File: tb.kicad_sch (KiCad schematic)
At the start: 66 parts, among them U4 JHL6340SLLSQ, U5 MX25L8006EM1I-12G, U6 SI52112-B6-GT, Y1 ABM8G-25.000MHZ-B4Y-T, Y2 ABM8G-25.000MHZ-B4Y-T

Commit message: Fixed all DRC errors and warnings, finished designators' placement
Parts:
- U5: footprint antmicro-footprints:SOIC-8_W3.9mm -> antmicro-footprints:SOIC-8_3.9x4.9x1.75mm_P1.27mm
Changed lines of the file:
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@@
       (effects (font (size 1.27 1.27) (thickness 0.15)) (justify left))
     )
-    (property "Footprint" "antmicro-footprints:SOIC-8_W3.9mm" (id 2) (at 39.37 384.81 0)
+    (property "Footprint" "antmicro-footprints:SOIC-8_3.9x4.9x1.75mm_P1.27mm" (id 2) (at 39.37 384.81 0)
       (effects (font (size 1.27 1.27) (thickness 0.15)) (justify left bottom) hide)
     )

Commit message: Bump revision, update naming
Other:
- title: (none) -> Thunderbolt to PCIe bridge
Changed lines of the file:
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@@
   (paper "A3" portrait)
   (title_block
-    (rev "0.99")
+    (title "Thunderbolt to PCIe bridge")
+    (date "2023-05-09")
+    (rev "1.0.0")
+    (comment 1 "www.antmicro.com")
+    (comment 2 "Antmicro Ltd.")
   )
   (junction (at 219.71 208.28) (diameter 0) (color 0 0 0 0)

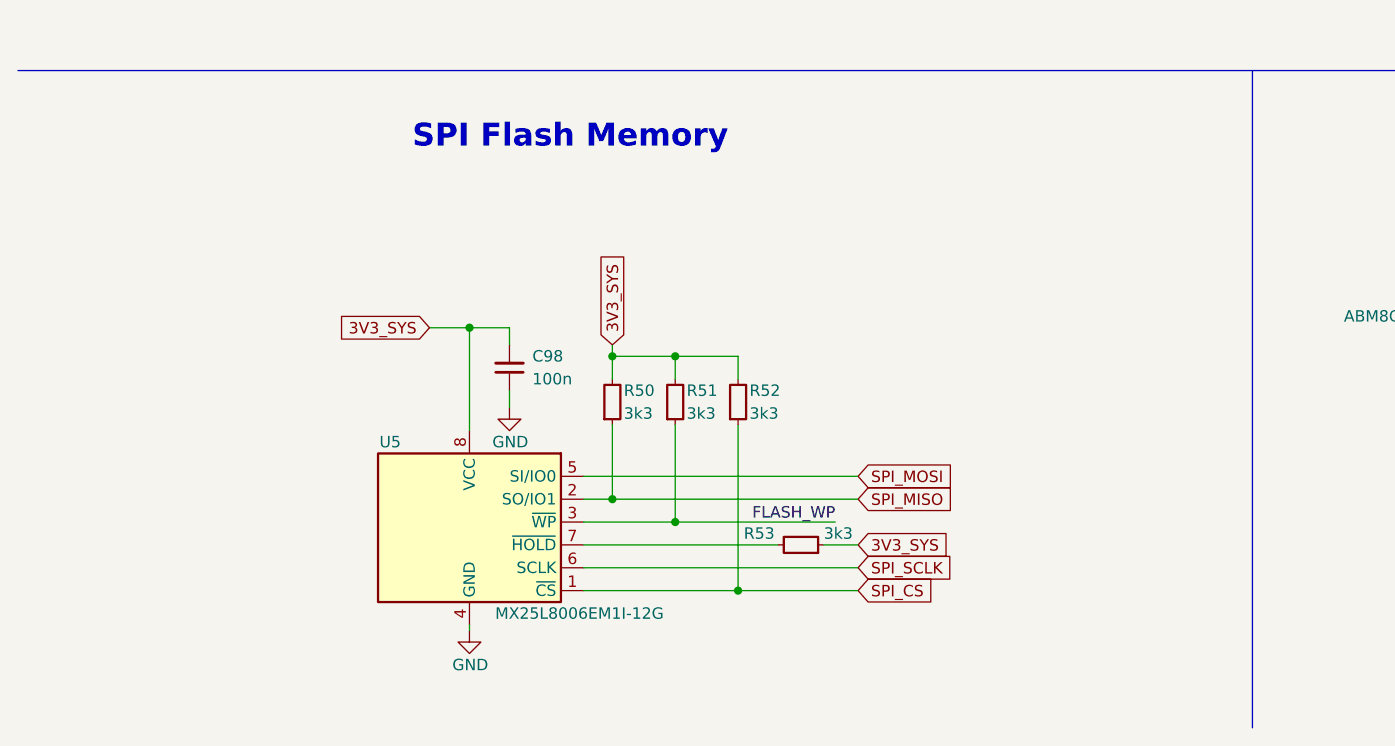
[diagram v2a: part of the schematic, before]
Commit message: Add option to use SPI flash in 200mils package
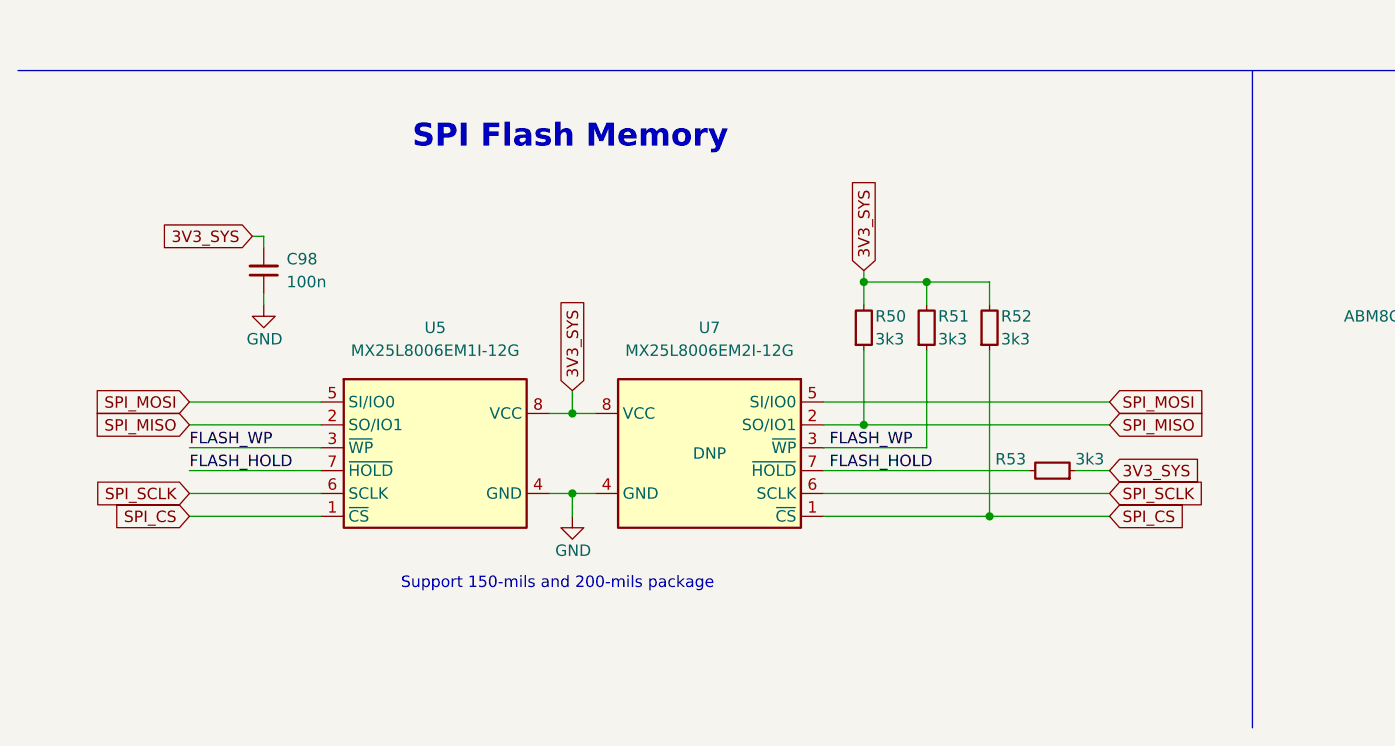
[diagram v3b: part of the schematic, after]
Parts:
- added U7: MX25L8006EM2I-12G, antmicro-footprints:SOIC-8_5.3x5.3x2mm_P1.27mm, symbol antmicroMemory:MX25L8006EM2I-12G
- U5: Author (none) -> Antmicro; License Apache-2.0 License -> Apache-2.0
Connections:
- net 3V3_SYS: now also U7.8 (VCC)
- net FLASH_WP: now also U7.3 (~{WP})
- net GND: now also U7.4 (GND)
- net SPI_CS: now also U7.1 (~{CS})
- net SPI_MISO: now also U7.2 (SO/IO1)
- net SPI_MOSI: now also U7.5 (SI/IO0)
- net SPI_SCLK: now also U7.6 (SCLK)
- net FLASH_HOLD: now reaches R53.2, U5.7 (~{HOLD})
- net FLASH_HOLD: now also U7.7 (~{HOLD})
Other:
- note added: "Support 150-mils and 200-mils package"
- moved on the sheet: C98, R50, R51, R52, R53, U5

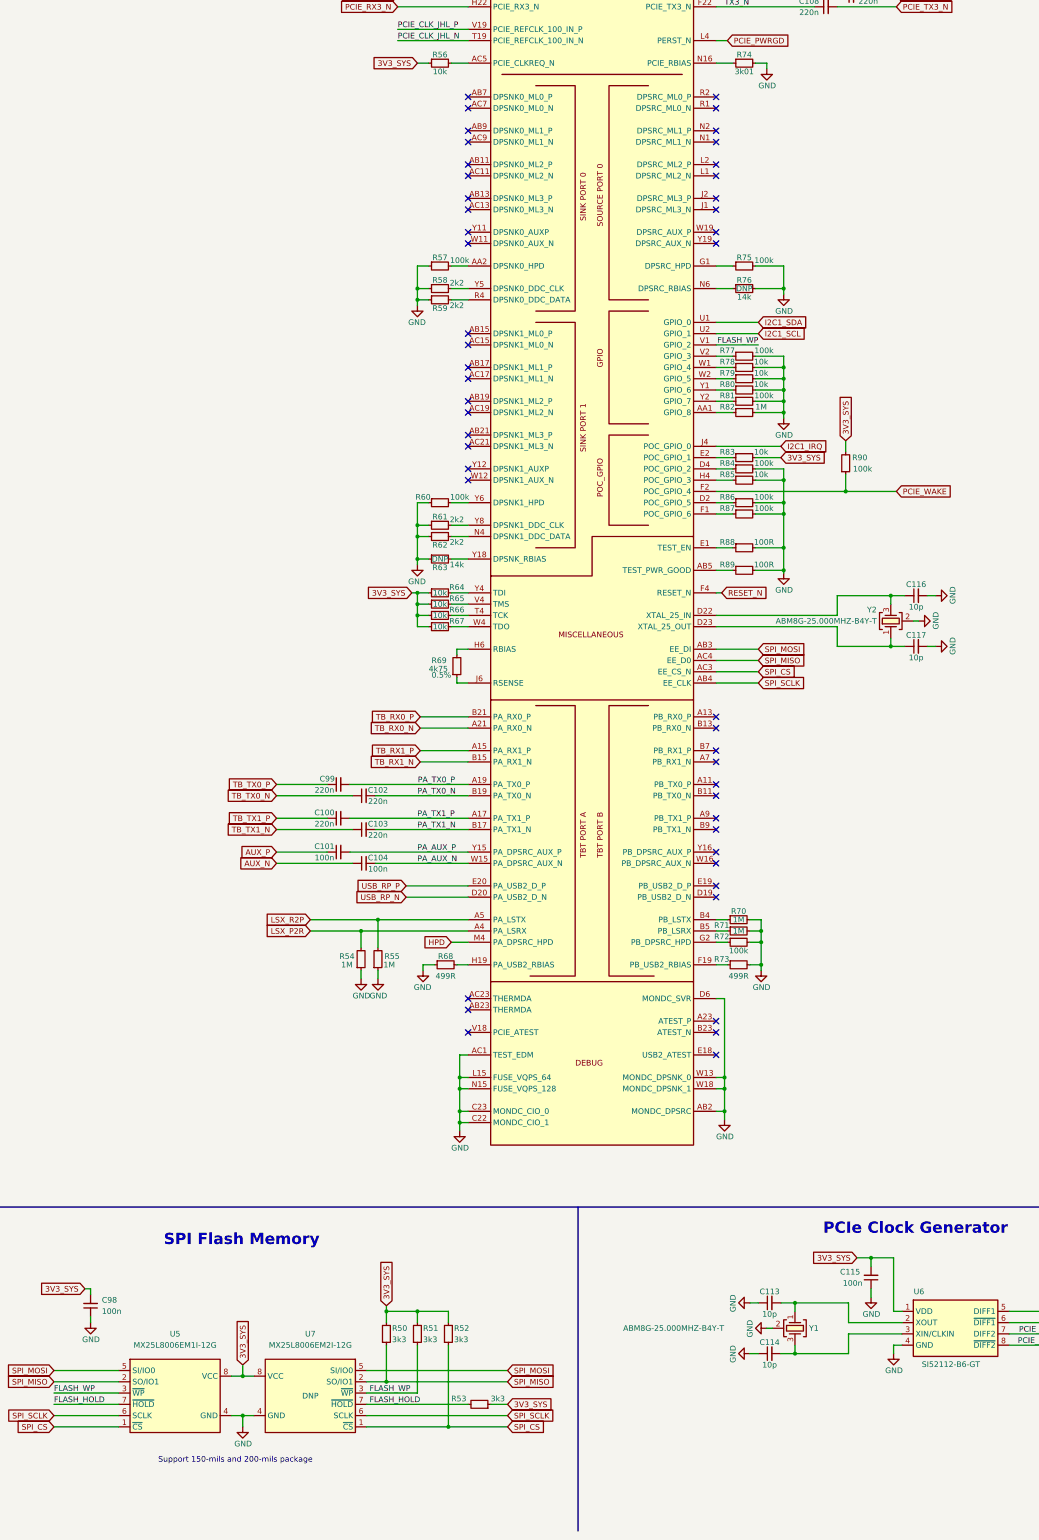
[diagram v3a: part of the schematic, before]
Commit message: Update all symbols from library to fix issues shown by klibs-check-license script
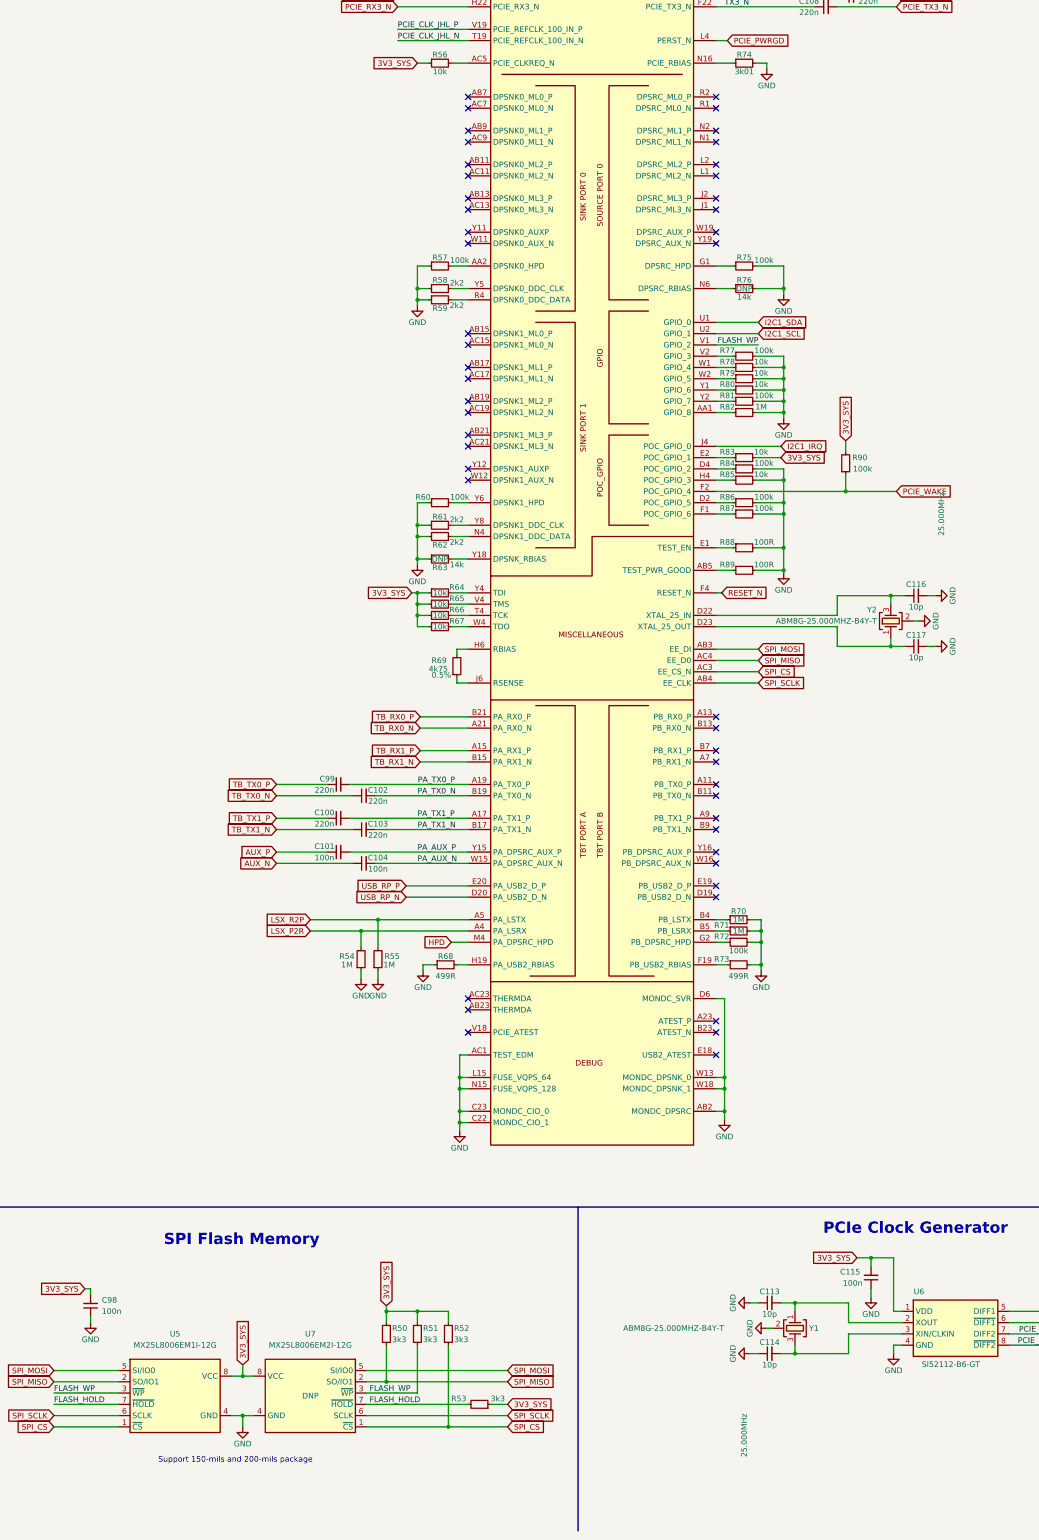
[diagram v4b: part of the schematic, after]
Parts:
- C100, C101, C102, C103, C104, C105, C106, C107, C108, C109, C110, C111, C112, C113, C114, C115, C116, C117, C98, C99, R50, R51, R52, R53, R54, R55, R56, R57, R58, R59, R60, R61, R62, R63, R64, R65, R66, R67, R68, R69, R70, R71, R72, R73, R74, R75, R76, R77, R78, R79, R80, R81, R82, R83, R84, R85, R86, R87, R88, R89, R90, U4, U6: Author (none) -> Antmicro; Copyright Copyright (c) 2023 Antmicro -> (none); License Apache-2.0 License -> Apache-2.0
- U5: Copyright Copyright (c) 2023 Antmicro -> (none)
- Y1, Y2: Author (none) -> Antmicro; Copyright Copyright (c) 2023 Antmicro -> (none); License Apache-2.0 License -> Apache-2.0; Val (none) -> 25.000MHz

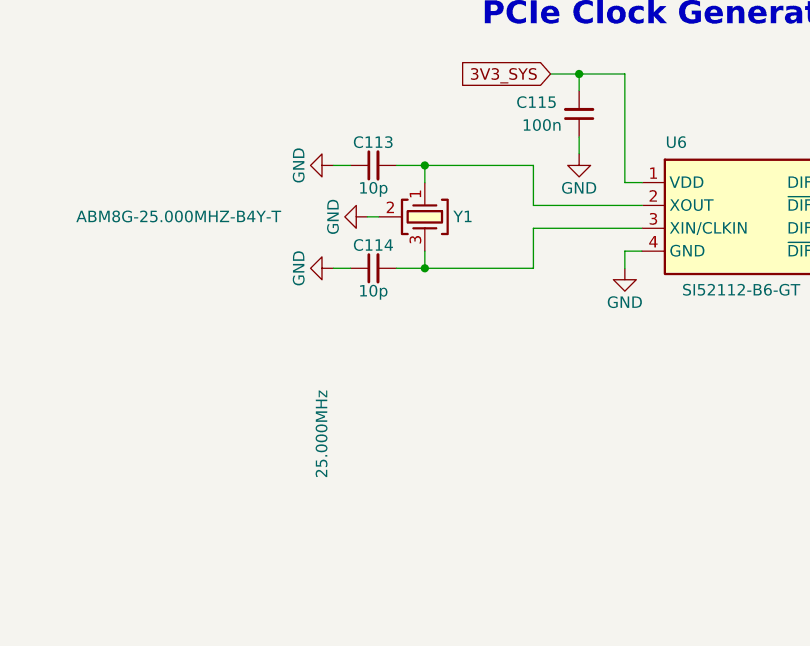
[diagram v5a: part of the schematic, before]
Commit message: Update naming convention
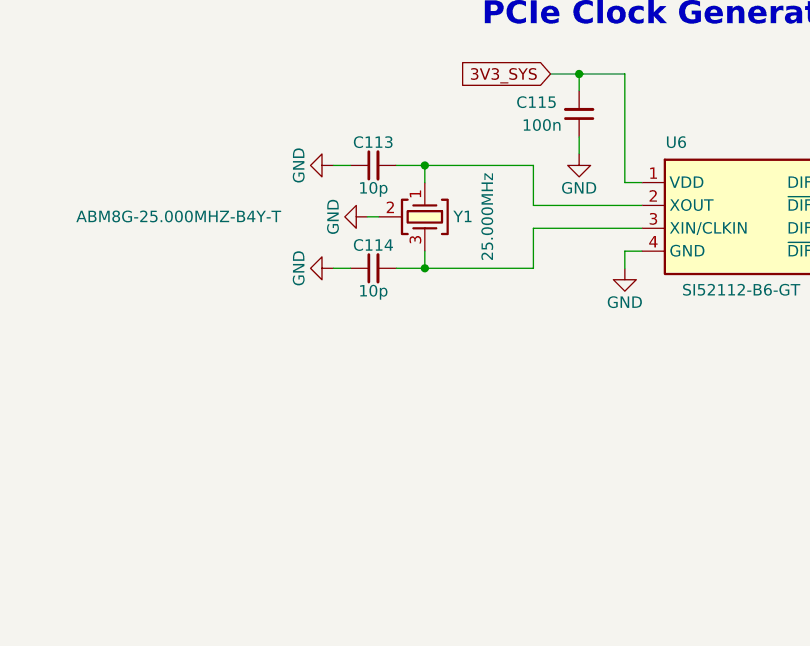
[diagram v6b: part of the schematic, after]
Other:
- title: Thunderbolt to PCIe bridge -> Thunderbolt PCIe Adaper
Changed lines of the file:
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@@
   (paper "A3" portrait)
   (title_block
-    (title "Thunderbolt to PCIe bridge")
-    (date "2023-05-09")
+    (title "Thunderbolt PCIe Adaper")
+    (date "2023-06-05")
     (rev "1.0.0")
     (comment 1 "www.antmicro.com")
@@
       (effects (font (size 1.27 1.27) (thickness 0.15)) (justify left bottom) hide)
     )
-    (property "Val" "25.000MHz" (id 9) (at 186.69 386.08 0))
-    (pin "1")
-    (pin "2")
+    (property "Val" "25.000MHz" (id 9) (at 205.105 361.95 0))
+    (pin "1")
+    (pin "2")

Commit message: Change symbol of U4, redraw schematic to use landscape orientation
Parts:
- removed U4: JHL6340SLLSQ, antmicro-footprints:JHL6340SLLSQ, symbol antmicroInterfaceControllers:JHL6340SLLSQ
- added U4: JHL6340SLLSQ, antmicro-footprints:JHL6340SLLSQ, symbol antmicroInterfaceControllers:JHL6340SLLSQ
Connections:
- net FLASH_WP: now also U4.V1 (GPIO_2)
- net GND: now also U4.AB2 (MONDC_DPSRC), U4.AC1 (TEST_EDM), U4.C22 (MONDC_CIO_1), U4.C23 (MONDC_CIO_0), U4.D6 (MONDC_SVR), U4.L15 (FUSE_VQPS_64), U4.N15 (FUSE_VQPS_128), U4.W13 (MONDC_DPSNK_0), U4.W18 (MONDC_DPSNK_1)
- net HPD: now also U4.M4 (PA_DPSRC_HPD)
- net I2C1_IRQ: now also U4.J4 (POC_GPIO_0)
- net I2C1_SCL: now also U4.U2 (GPIO_1)
- net I2C1_SDA: now also U4.U1 (GPIO_0)
- net LSX_P2R: now also U4.A4 (PA_LSRX)
- net LSX_R2P: now also U4.A5 (PA_LSTX)
- net PA_AUX_N: now also U4.W15 (PA_DPSRC_AUX_N)
- net PA_AUX_P: now also U4.Y15 (PA_DPSRC_AUX_P)
- net PA_TX0_N: now also U4.B19 (PA_TX0_N)
- net PA_TX0_P: now also U4.A19 (PA_TX0_P)
- net PA_TX1_N: now also U4.B17 (PA_TX1_N)
- net PA_TX1_P: now also U4.A17 (PA_TX1_P)
- net PCIE_CLK_JHL_N: now also U4.T19 (PCIE_REFCLK_100_IN_N)
- net PCIE_CLK_JHL_P: now also U4.V19 (PCIE_REFCLK_100_IN_P)
- net PCIE_PWRGD: now also U4.L4 (PERST_N)
- net PCIE_RX0_N: now also U4.Y22 (PCIE_RX0_N)
- net PCIE_RX0_P: now also U4.Y23 (PCIE_RX0_P)
- net PCIE_RX1_N: now also U4.T22 (PCIE_RX1_N)
- net PCIE_RX1_P: now also U4.T23 (PCIE_RX1_P)
- net PCIE_RX2_N: now also U4.M22 (PCIE_RX2_N)
- net PCIE_RX2_P: now also U4.M23 (PCIE_RX2_P)
- net PCIE_RX3_N: now also U4.H22 (PCIE_RX3_N)
- net PCIE_RX3_P: now also U4.H23 (PCIE_RX3_P)
- net PCIE_WAKE: now also U4.F2 (POC_GPIO_4)
- net RESET_N: now also U4.F4 (RESET_N)
- net SPI_CS: now also U4.AC3 (EE_CS_N)
- net SPI_MISO: now also U4.AC4 (EE_D0)
- net SPI_MOSI: now also U4.AB3 (EE_DI)
- net SPI_SCLK: now also U4.AB4 (EE_CLK)
- net TB_RX0_N: now also U4.A21 (PA_RX0_N)
- net TB_RX0_P: now also U4.B21 (PA_RX0_P)
- net TB_RX1_N: now also U4.B15 (PA_RX1_N)
- net TB_RX1_P: now also U4.A15 (PA_RX1_P)
- net TX0_N: now also U4.V22 (PCIE_TX0_N)
- net TX0_P: now also U4.V23 (PCIE_TX0_P)
- net TX1_N: now also U4.P22 (PCIE_TX1_N)
- net TX1_P: now also U4.P23 (PCIE_TX1_P)
- net TX2_N: now also U4.K22 (PCIE_TX2_N)
- net TX2_P: now also U4.K23 (PCIE_TX2_P)
- net TX3_N: now also U4.F22 (PCIE_TX3_N)
- net TX3_P: now also U4.F23 (PCIE_TX3_P)
- net USB_RP_N: now also U4.D20 (PA_USB2_D_N)
- net USB_RP_P: now also U4.E20 (PA_USB2_D_P)
- net at R74.1: now also U4.N16 (PCIE_RBIAS)
- net at R58.2: now also U4.Y5 (DPSNK0_DDC_CLK)
- net at R62.2: now also U4.N4 (DPSNK1_DDC_DATA)
- net at C117.1, Y2.1: now also U4.D23 (XTAL_25_OUT)
- net at C116.1, Y2.3: now also U4.D22 (XTAL_25_IN)
- net at R84.1: now also U4.D4 (POC_GPIO_2)
- net at R69.1: now also U4.J6 (RSENSE)
- net at R69.2: now also U4.H6 (RBIAS)
- net at R79.1: now also U4.W2 (GPIO_5)
- net at R65.2: now also U4.V4 (TMS)
- net at R78.1: now also U4.W1 (GPIO_4)
- net at R80.1: now also U4.Y1 (GPIO_6)
- net at R70.1: now also U4.B4 (PB_LSTX)
- net at R57.2: now also U4.AA2 (DPSNK0_HPD)
- net at R67.2: now also U4.W4 (TDO)
- net at R81.1: now also U4.Y2 (GPIO_7)
- net at R82.1: now also U4.AA1 (GPIO_8)
- net at R89.1: now also U4.AB5 (TEST_PWR_GOOD)
- net at R56.2: now also U4.AC5 (PCIE_CLKREQ_N)
- net at R71.1: now also U4.B5 (PB_LSRX)
- net at R86.1: now also U4.D2 (POC_GPIO_5)
- net at R88.1: now also U4.E1 (TEST_EN)
- net at R83.1: now also U4.E2 (POC_GPIO_1)
- net at R87.1: now also U4.F1 (POC_GPIO_6)
- net at R73.1: now also U4.F19 (PB_USB2_RBIAS)
- net at R75.1: now also U4.G1 (DPSRC_HPD)
- net at R72.1: now also U4.G2 (PB_DPSRC_HPD)
- net at R68.2: now also U4.H19 (PA_USB2_RBIAS)
- net at R85.1: now also U4.H4 (POC_GPIO_3)
- net at R76.1: now also U4.N6 (DPSRC_RBIAS)
- net at R59.2: now also U4.R4 (DPSNK0_DDC_DATA)
- net at R66.2: now also U4.T4 (TCK)
- net at R77.1: now also U4.V2 (GPIO_3)
- net at R63.2: now also U4.Y18 (DPSNK_RBIAS)
- net at R64.2: now also U4.Y4 (TDI)
- net at R60.2: now also U4.Y6 (DPSNK1_HPD)
- net at R61.2: now also U4.Y8 (DPSNK1_DDC_CLK)
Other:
- note added: "DisplayPorts"
- note added: "PCIe x4 Gen3"
- note added: "Thunderbolt Controller Debug"
- note added: "Thunderbolt Controller Misc"
- moved on the sheet: C100, C101, C102, C103, C104, C105, C106, C107, C108, C109, C110, C111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
